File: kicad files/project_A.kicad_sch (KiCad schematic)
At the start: 14 parts, among them M1 Motor_Servo, M2 Motor_Servo, M3 Motor_DC, SW1 SW_Push, SW2 SW_Push, U1 SC39-12EWA, U2 SC39-12EWA, U3 74HC595, U4 74HC595

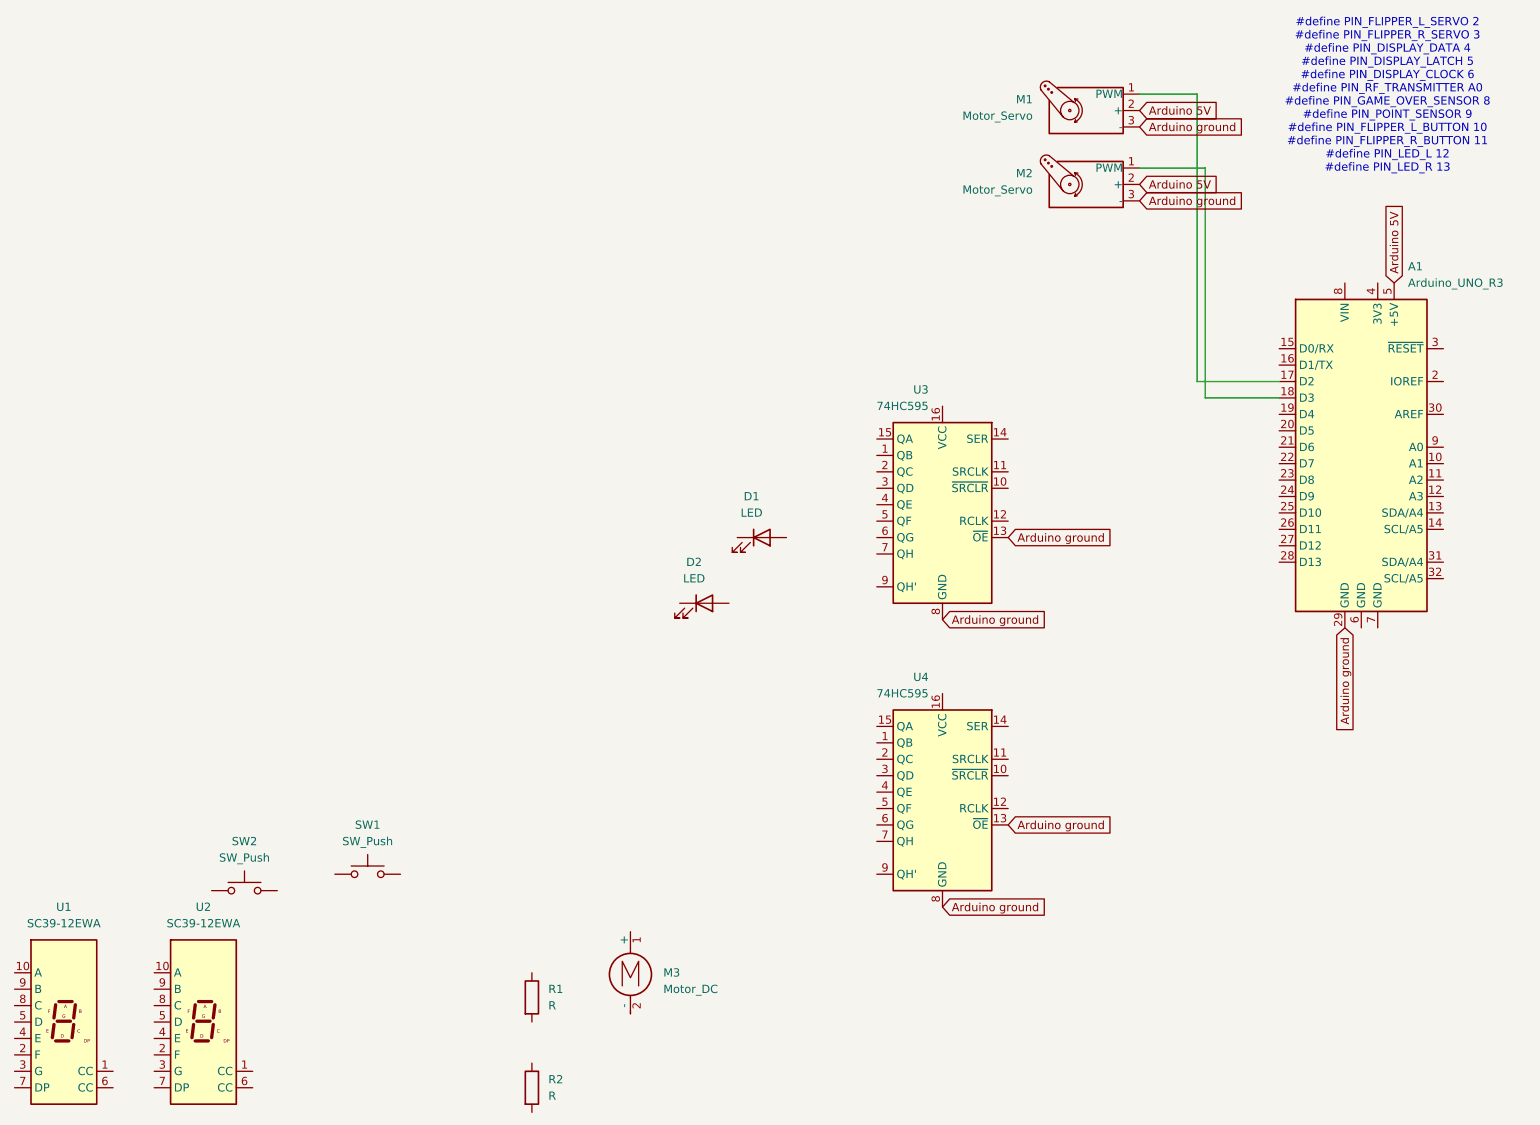
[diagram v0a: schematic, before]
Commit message: verdere updates
toevoeging van 3d file en aanpassing kicad files
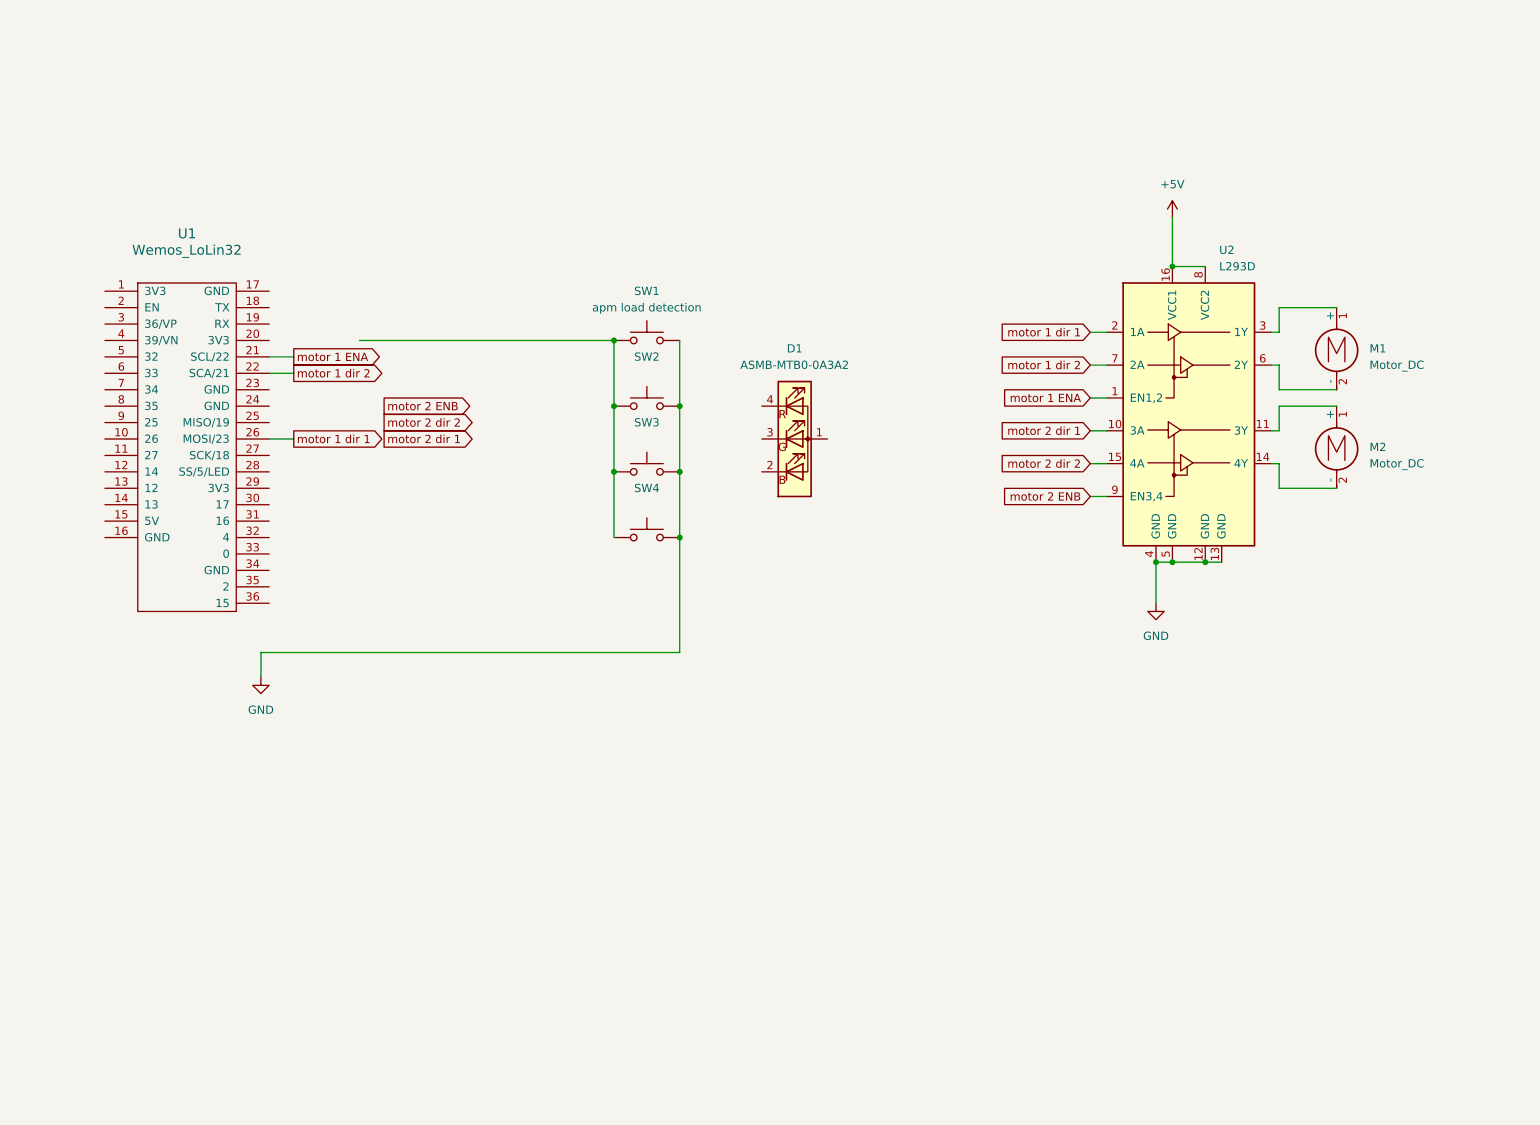
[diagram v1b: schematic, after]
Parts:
- removed A1: Arduino_UNO_R3, Module:Arduino_UNO_R3, symbol MCU_Module:Arduino_UNO_R3
- removed D1, D2: LED, symbol Device:LED
- removed M1, M2: Motor_Servo, symbol Motor:Motor_Servo
- removed M3: Motor_DC, symbol Motor:Motor_DC
- removed R1, R2: R, symbol Device:R
- removed U1, U2: SC39-12EWA, Display_7Segment:Sx39-1xxxxx, symbol Display_Character:SC39-12EWA
- removed U3, U4: 74HC595, symbol 74xx:74HC595
- added D1: ASMB-MTB0-0A3A2, LED_SMD:LED_Avago_PLCC4_3.2x2.8mm_CW, symbol LED:ASMB-MTB0-0A3A2
- added M1, M2: Motor_DC, symbol Motor:Motor_DC
- added SW3, SW4: apm load detection, symbol Switch:SW_Push
- added U1: Wemos_LoLin32, symbol wemos:Wemos_LoLin32
- added U2: L293D, Package_DIP:DIP-16_W7.62mm, symbol Driver_Motor:L293D
- SW1, SW2: value SW_Push -> apm load detection
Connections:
- net at SW2.1: now also SW1.1, SW3.1, SW4.1
- net GND: now reaches SW2.2
- net GND: now also SW1.2, SW3.2, SW4.2, U2.12 (GND), U2.13 (GND), U2.4 (GND), U2.5 (GND)
- new net: M1.1 (+), U2.3 (1Y)
- new net: M1.2 (-), U2.6 (2Y)
- new net: M2.1 (+), U2.11 (3Y)
- new net: M2.2 (-), U2.14 (4Y)
- new net +5V: U2.16 (VCC1), U2.8 (VCC2)
- new net motor 1 ENA: U1.21 (SCL/22), U2.1 (EN1,2)
- new net motor 1 dir 1: U1.26 (MOSI/23), U2.2 (1A)
- new net motor 1 dir 2: U1.22 (SCA/21), U2.7 (2A)
- new net motor 2 ENB: U2.9 (EN3,4)
- new net motor 2 dir 1: U2.10 (3A)
- new net motor 2 dir 2: U2.15 (4A)
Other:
- note removed: "#define PIN_FLIPPER_L_SERVO 2 #define PIN_FLIPPER_R_SERVO 3 #define PIN_DISPLAY_DATA 4 #define PIN_DISPLAY_LATCH 5 #define PIN_DISPLAY_CLOCK 6 #define PIN_RF_TRANSMITTER A0 #define PIN_GAME_OVER_SENSOR 8 #define PIN_POINT_SENSOR 9 #define PIN_FLIPPER_L_BUTTON 10 #define PIN_FLIPPER_R_BUTTON 11 #define PIN_LED_L 12 #define PIN_LED_R 13"
